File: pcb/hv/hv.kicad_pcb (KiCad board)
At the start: 2 copper layers, 85 x 55 mm, 49 parts, among them J1 JST XH, J2 Phoenix MSTB, Q1 IRL540N, Q2 TN2106N3-G, T1 >VALUE, U1 LM5156H

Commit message: Improve several 3D models, design testing base plate
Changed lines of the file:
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@@
 	(property "AUTHOR" "Jason Watkins")
 	(property "REV" "C")
-	(property "STEP" "1")
+	(property "STEP" "3")
 	(property "TITLE" "170V Flyback Converter")
 	(footprint "Diode_THT:D_DO-41_SOD81_P10.16mm_Horizontal"
@@
 			)
 		)
+		(fp_text user "K"
+			(at 0 -2.1 270)
+			(layer "F.Fab")
+			(effects
+				(font
+					(size 1 1)
+					(thickness 0.15)
+				)
+			)
+		)
 		(pad "1" thru_hole roundrect
 			(at 0 0 270)
@@
 			(layer "F.Fab")
 		)
+		(fp_text user "K"
+			(at 0 -1.8 270)
+			(layer "F.SilkS")
+			(effects
+				(font
+					(size 1 1)
+					(thickness 0.15)
+				)
+			)
+		)
 		(fp_text user "${REFERENCE}"
 			(at 4.11 0 90)
@@
 			)
 		)
+		(fp_text user "K"
+			(at 0 -2.1 90)
+			(layer "F.Fab")
+			(effects
+				(font
+					(size 1 1)
+					(thickness 0.15)
+				)
+			)
+		)
 		(fp_text user "${REFERENCE}"
 			(at 4.2 0 90)
@@
 		(sheetname "/")
 		(sheetfile "hv.kicad_sch")
-		(zone_connect 2)
 		(attr smd)
 		(duplicate_pad_numbers_are_jumpers no)
@@
 		)
 		(fp_text user "K"
+			(at 0 -2.1 90)
+			(layer "F.SilkS")
+			(effects
+				(font
+					(size 1 1)
+					(thickness 0.15)
+				)
+			)
+		)
+		(fp_text user "K"

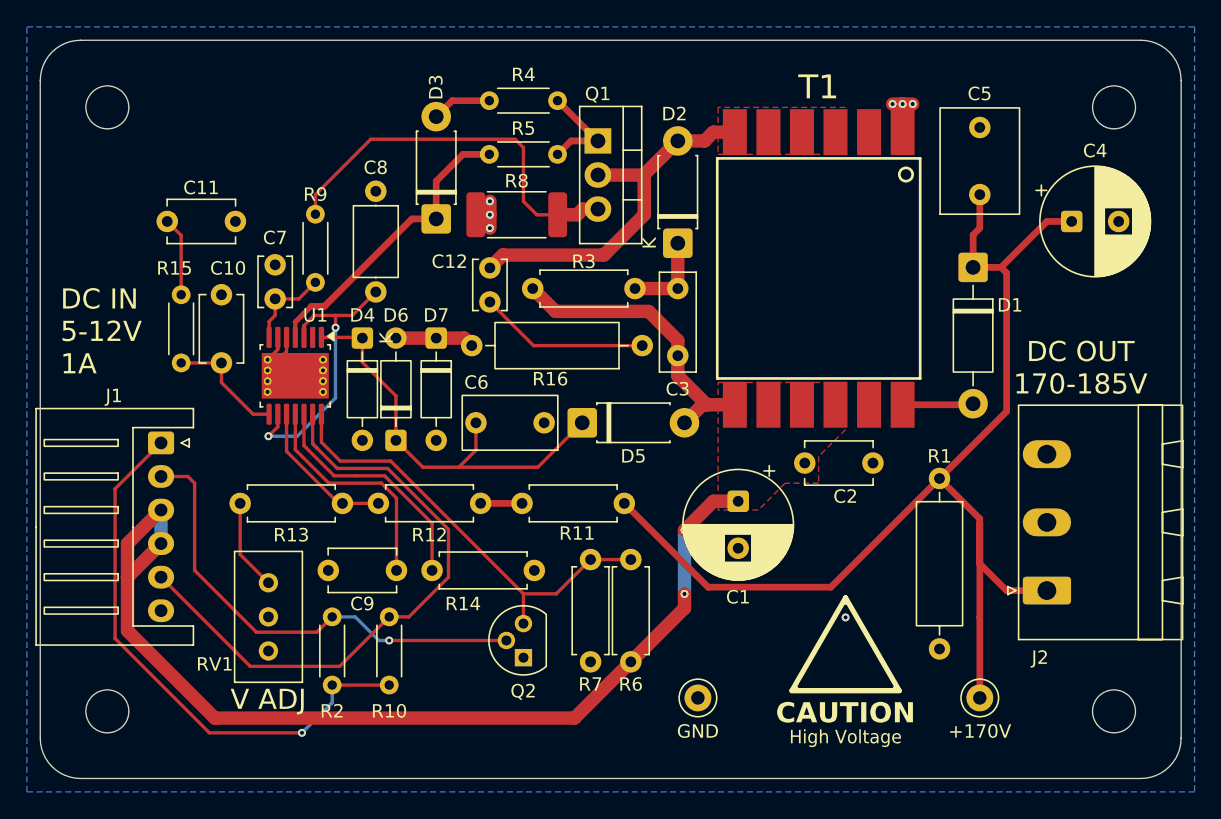
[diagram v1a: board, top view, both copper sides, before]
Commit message: Update ins1 tube model, update hv/main connector to 1 vbus, 2 gnd connections, update hv inhibit circuit to be default inhibit and require positive enable from MCU
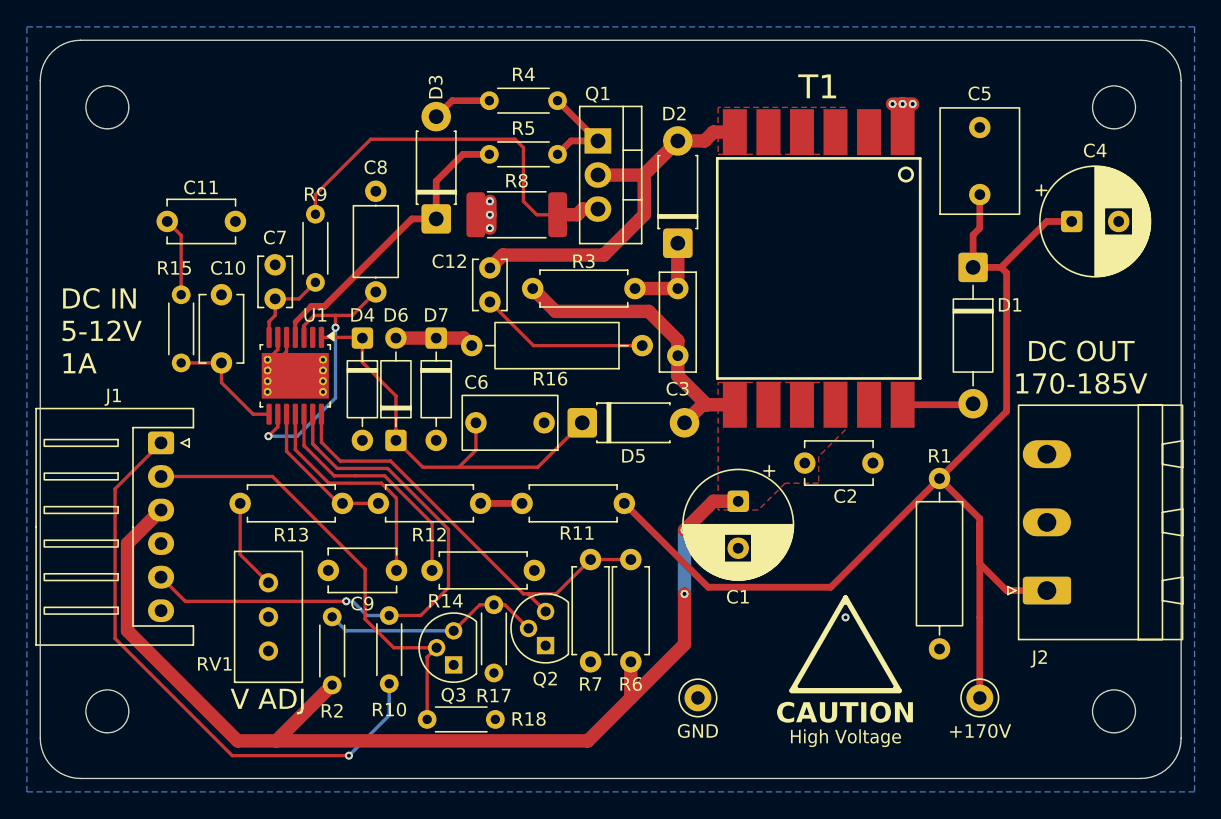
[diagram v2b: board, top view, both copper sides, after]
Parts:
- added Q3: TN2106N3-G, Package_TO_SOT_THT:TO-92L, F.Cu at (135.8, 121.5)
- added R17: 1M, Resistor_THT:R_Axial_DIN0204_L3.6mm_D1.6mm_P5.08mm_Horizontal, F.Cu at (138.8, 117.1)
- added R18: 100k, Resistor_THT:R_Axial_DIN0204_L3.6mm_D1.6mm_P5.08mm_Horizontal, F.Cu at (133.8, 125.6)
- R13: value 8.25k -> 9.09k
- T1: value >VALUE -> DA2032-AL
- moved Q2 1.88 mm to (142.7, 120.1)
- moved R10 0.10 mm to (131.0, 122.9)
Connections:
- J1 pad 2: ~{EN}_{HV} -> EN_{HV}
- J1 pad 4: V_{BUS} -> GND
- Q2 pad 2: ~{EN}_{HV} -> Net-(Q2-G)
- R2 pad 1: +3V3 -> V_{BUS}
- R2 pad 2: ~{EN}_{HV} -> Net-(Q2-G)
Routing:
- net ~{EN}_{HV}: track 35.5 -> 0.00 mm, vias 1 -> 0
- net EN_{HV}: track 0.00 -> 33.6 mm
- net Net-(Q2-G): track 0.00 -> 16.6 mm
- net V_{BUS}: track 97.1 -> 102.6 mm
- net PGOOD_{HV}: track 45.8 -> 43.1 mm, vias 0 -> 1
- net +3V3: track 41.6 -> 43.6 mm
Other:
- board text added: "Enable"
- board text removed: "Inhibit"
